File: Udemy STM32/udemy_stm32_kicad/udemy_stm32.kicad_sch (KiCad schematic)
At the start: 13 parts

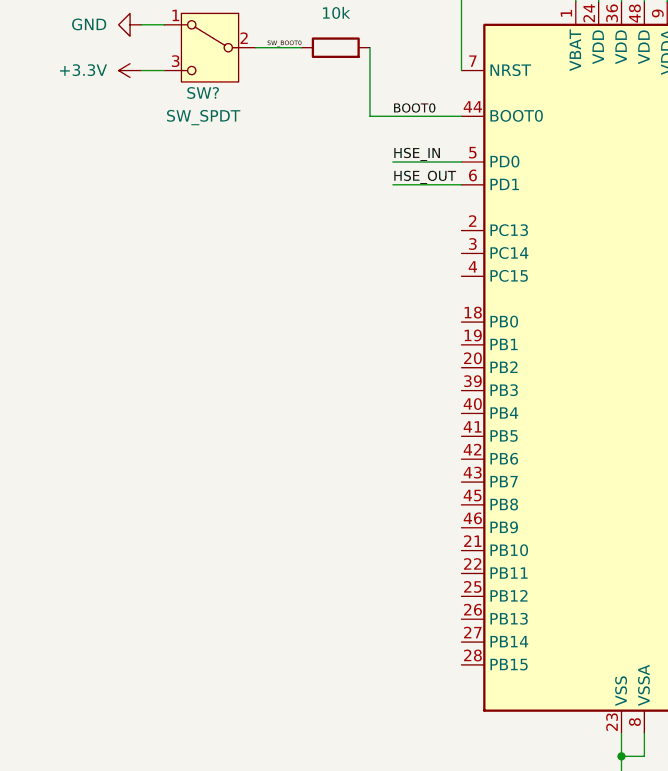
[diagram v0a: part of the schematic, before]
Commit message: Crystal added
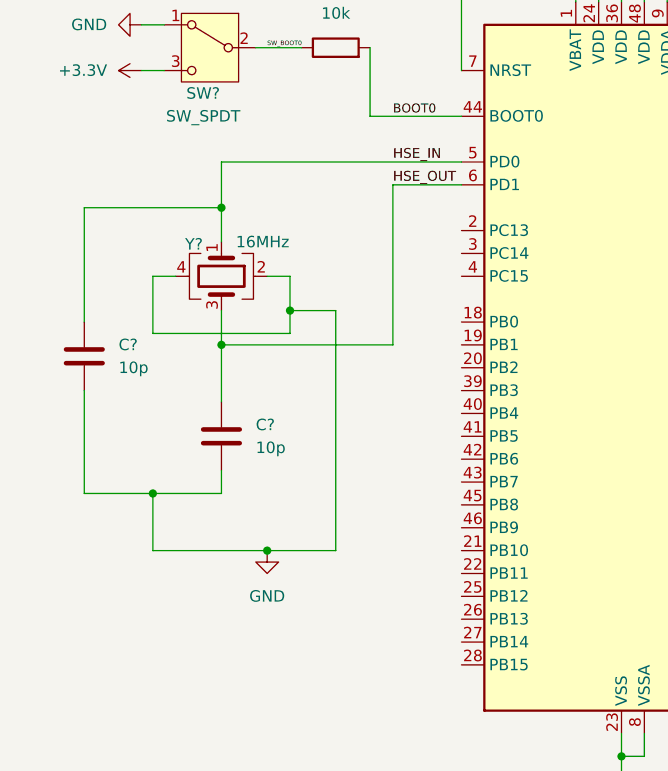
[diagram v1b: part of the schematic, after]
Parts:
- added C? (x2): 10p, symbol Device:C
- added Y?: 16MHz, symbol Device:Crystal_GND24
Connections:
- net GND: now also C?.2, C?.2, Y?.2, Y?.4
- net HSE_IN: now also C?.1, Y?.1
- net HSE_OUT: now also C?.1, Y?.3

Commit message: Schematic and footprint completed
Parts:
- added C1, C2: 22u, Capacitor_SMD:C_0805_2012Metric, symbol Device:C
- added D1: LED, LED_SMD:LED_0603_1608Metric, symbol Device:LED
- added J1, J2, J3: Conn_01x04_Pin, Connector_PinHeader_2.54mm:PinHeader_1x04_P2.54mm_Vertical, symbol Connector:Conn_01x04_Pin
- added J4: USB_B_Micro, Connector_USB:USB_Micro-B_Wuerth_629105150521, symbol Connector:USB_B_Micro
- added R1, R2, R4, R5: 1.5k, Resistor_SMD:R_0402_1005Metric, symbol Device:R
- added U1: AMS1117-3.3, Package_TO_SOT_SMD:SOT-223-3_TabPin2, symbol Regulator_Linear:AMS1117-3.3
- C10, C11, C12, C13, C3, C5, C6, C7, C8, C9: renamed from C?; footprint (none) -> Capacitor_SMD:C_0402_1005Metric
- C4: renamed from C?; footprint (none) -> Capacitor_SMD:C_0603_1608Metric
- FB1: renamed from FB?; footprint (none) -> Inductor_SMD:L_0603_1608Metric
- R3: renamed from R?; footprint (none) -> Resistor_SMD:R_0402_1005Metric
- SW1: renamed from SW?; footprint (none) -> Button_Switch_THT:SW_E-Switch_EG1224_SPDT_Angled
- Y1: renamed from Y?; footprint (none) -> Crystal:Crystal_SMD_3225-4Pin_3.2x2.5mm
- gave numbers to parts that had none: 1
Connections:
- net +3.3V: now also C2.1, D1.2 (A), J1.1 (Pin_1), J2.1 (Pin_1), J3.1 (Pin_1), R2.2, R4.2, R5.2, U1.2 (VO)
- net GND: now also C1.2, C2.2, J1.4 (Pin_4), J2.4 (Pin_4), J3.4 (Pin_4), J4.5 (GND), R1.2, U1.1 (GND)
- net SWCLK: now also J3.3 (Pin_3)
- net SWDIO: now also J3.2 (Pin_2)
- net USB_D+: now also J4.3 (D+), R5.1
- net USB_D-: now also J4.2 (D-)
- net UART2_TX: now reaches U2.20 (PB2)
- net UART2_TX: now also J1.2 (Pin_2)
- net UART2_TRX: now reaches U2.39 (PB3)
- net UART2_TRX: now also J1.3 (Pin_3)
- net I2C1_SCL: now reaches U2.42 (PB6)
- net I2C1_SCL: now also J2.3 (Pin_3), R2.1
- net I2C1_SDA: now reaches U2.43 (PB7)
- net I2C1_SDA: now also J2.2 (Pin_2), R4.1
- new net: D1.1 (K), R1.1
- new net VBUS: C1.1, J4.1 (VBUS), U1.3 (VI)
- no-connect marks 0 -> 29
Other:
- note added: "Microcontroller"
- note added: "Power Supply"
- company: (none) -> Fardin's Tech
- title: (none) -> Udemy STM32
- moved on the sheet: C10, C11, C12, C13, C3, C4, C5, C6, C7, C8, C9, FB1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

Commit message: PCB rough design half done
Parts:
- SW1: footprint Button_Switch_THT:SW_E-Switch_EG1224_SPDT_Angled -> Button_Switch_SMD:SW_SPDT_PCM12
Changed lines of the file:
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@@
 			)
 		)
-		(property "Footprint" "Button_Switch_THT:SW_E-Switch_EG1224_SPDT_Angled"
+		(property "Footprint" "Button_Switch_SMD:SW_SPDT_PCM12"
 			(at 132.08 50.8 0)
 			(effects

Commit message: Tinkering around for good placements
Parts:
- added H1, H2, H3, H4: MountingHole, MountingHole:MountingHole_2.2mm_M2, symbol Mechanical:MountingHole
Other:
- note added: "Mounting holes"
